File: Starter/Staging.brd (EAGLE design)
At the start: 20 x 20 mm, 2 parts, among them J1 DF40.30PIN.RECEPTACLE, J3 DF40.30PIN.HEADER

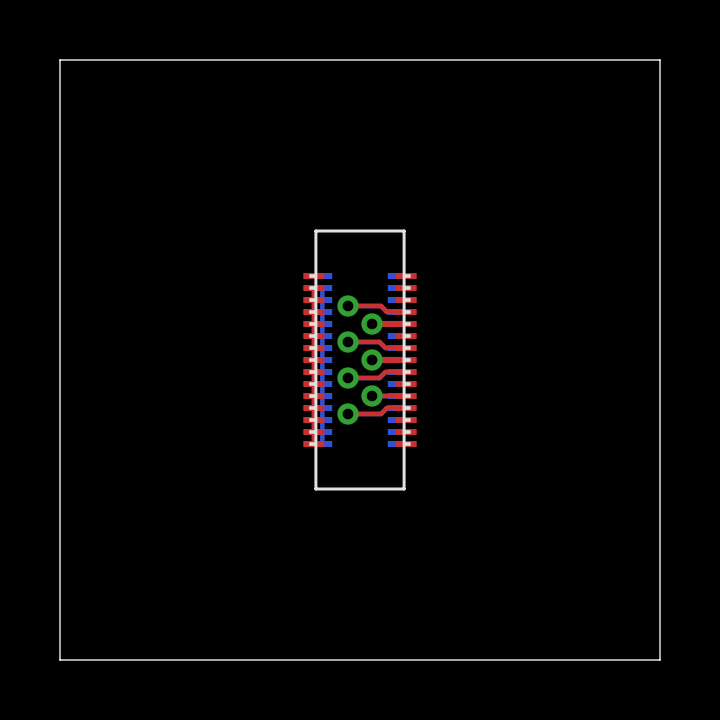
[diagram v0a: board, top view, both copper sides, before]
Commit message: More work on new headers. Focusing on H1, and it's various IO schemes.
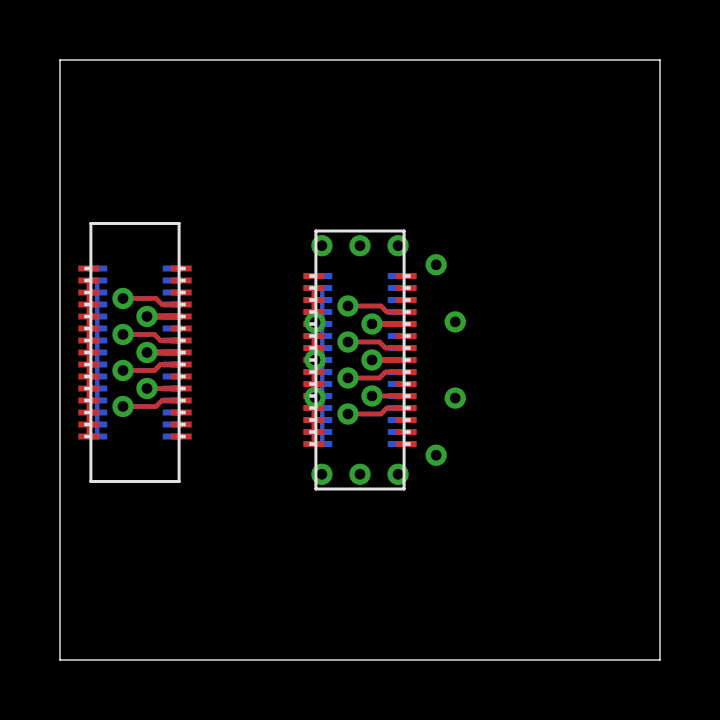
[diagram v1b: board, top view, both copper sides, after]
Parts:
- added H1: ROOT1.H1.BOTH.PASSTHROUGH, anomalousmaker:ROOT1.H1.BOTH
- moved J1 7.50 mm to (2.50, 10.2)
- moved J3 7.50 mm to (2.50, 10.2)
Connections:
- new net N$1: H1.IO.7.BOTTOM, H1.IO.7.TOP, H1.IO.7.VIA
- new net N$10: H1.GND@0.BOTTOM, H1.GND@0.TOP, H1.GND@0.VIA, H1.GND@1.BOTTOM, H1.GND@1.TOP, H1.GND@1.VIA, H1.GND@10.BOTTOM, H1.GND@10.TOP, H1.GND@11.BOTTOM, H1.GND@11.TOP, H1.GND@12.BOTTOM, H1.GND@12.TOP, H1.GND@13.BOTTOM, H1.GND@13.TOP, H1.GND@2.BOTTOM, H1.GND@2.TOP, H1.GND@2.VIA, H1.GND@3.BOTTOM, H1.GND@3.TOP, H1.GND@3.VIA, H1.GND@4.BOTTOM, H1.GND@4.TOP, H1.GND@5.BOTTOM, H1.GND@5.TOP, H1.GND@6.BOTTOM, H1.GND@6.TOP, H1.GND@7.BOTTOM, H1.GND@7.TOP, H1.GND@8.BOTTOM, H1.GND@8.TOP, H1.GND@9.BOTTOM, H1.GND@9.TOP
- new net N$11: H1.ADC0.BOTTOM, H1.ADC0.TOP, H1.ADC0.VIA
- new net N$12: H1.ADC1.BOTTOM, H1.ADC1.TOP, H1.ADC1.VIA
- new net N$13: H1.TX0.VIA, H1.TXO.BOTTOM, H1.TXO.TOP
- new net N$14: H1.RXI.BOTTOM, H1.RXI.TOP, H1.RXI.VIA
- new net N$15: H1.MOSI.BOTTOM, H1.MOSI.TOP, H1.MOSI.VIA
- new net N$16: H1.MISO.BOTTOM, H1.MISO.TOP, H1.MISO.VIA
- new net N$17: H1.SCLK.BOTTOM, H1.SCLK.TOP, H1.SCLK.VIA
- new net N$2: H1.IO.6.BOTTOM, H1.IO.6.TOP, H1.IO.6.VIA
- new net N$3: H1.IO.5.BOTTOM, H1.IO.5.TOP, H1.IO.5.VIA
- new net N$4: H1.IO.4.BOTTOM, H1.IO.4.TOP, H1.IO.4.VIA
- new net N$5: H1.IO.3.BOTTOM, H1.IO.3.TOP, H1.IO.3.VIA
- new net N$6: H1.IO.2.BOTTOM, H1.IO.2.TOP, H1.IO.2.VIA
- new net N$7: H1.IO.1.BOTTOM, H1.IO.1.TOP, H1.IO.1.VIA
- new net N$8: H1.IO.0.BOTTOM, H1.IO.0.TOP, H1.IO.0.VIA
- new net N$9: H1.!RST!.BOTTOM, H1.!RST!.TOP, H1.!RST!.VIA

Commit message: Created Test Module to test out Samtec SSH, STH, and SEI headers, along with EEPROM/Loki Scheme, and breakable PCB idea.
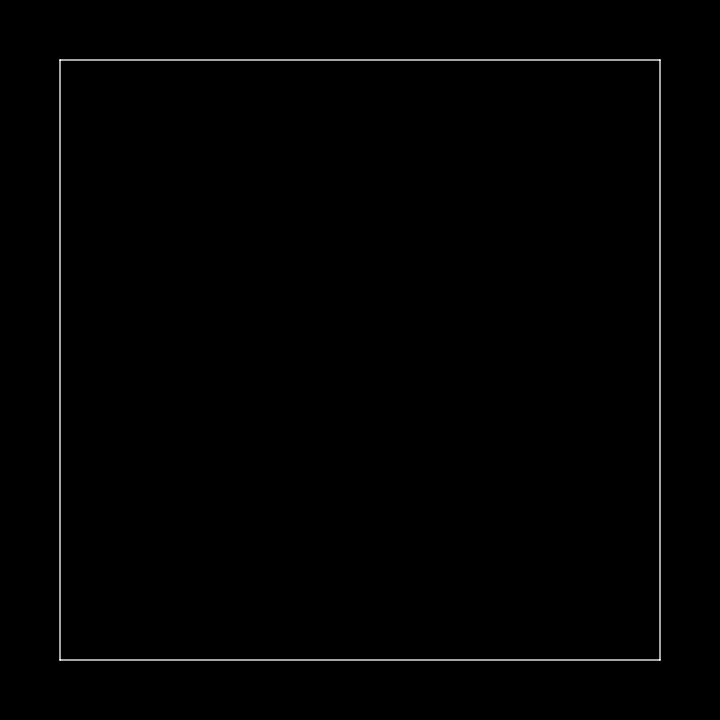
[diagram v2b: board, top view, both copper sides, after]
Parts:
- removed H1: ROOT1.H1.BOTH.PASSTHROUGH, anomalousmaker:ROOT1.H1.BOTH
- removed J1: DF40.30PIN.RECEPTACLE, hirose:DF40(XX)-30DS-0.4V
- removed J3: DF40.30PIN.HEADER, hirose:DF40(XX)-30DP-0.4V
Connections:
- removed net ADC0: J1.2, J3.30
- removed net ADC1: J1.4, J3.28
- removed net GND: J1.11, J1.13, J1.15, J1.17, J1.19, J1.21, J1.23, J1.25, J1.27, J1.29, J1.3, J1.5, J1.7, J1.9, J3.1, J3.11, J3.13, J3.15, J3.17, J3.19, J3.21, J3.23, J3.25, J3.27, J3.3, J3.5, J3.7, J3.9
- removed net IO.0: J1.16, J3.16
- removed net IO.1: J1.18, J3.14
- removed net IO.2: J1.20, J3.12
- removed net IO.3: J1.22, J3.10
- removed net IO.4: J1.24, J3.8
- removed net IO.5: J1.26, J3.6
- removed net IO.6: J1.28, J3.4
- removed net IO.7: J1.30, J3.2
- removed net MISO: J1.12, J3.20
- removed net MOSI: J1.10, J3.22
- removed net N$1: H1.IO.7.BOTTOM, H1.IO.7.TOP, H1.IO.7.VIA
- removed net N$10: H1.GND@0.BOTTOM, H1.GND@0.TOP, H1.GND@0.VIA, H1.GND@1.BOTTOM, H1.GND@1.TOP, H1.GND@1.VIA, H1.GND@10.BOTTOM, H1.GND@10.TOP, H1.GND@11.BOTTOM, H1.GND@11.TOP, H1.GND@12.BOTTOM, H1.GND@12.TOP, H1.GND@13.BOTTOM, H1.GND@13.TOP, H1.GND@2.BOTTOM, H1.GND@2.TOP, H1.GND@2.VIA, H1.GND@3.BOTTOM, H1.GND@3.TOP, H1.GND@3.VIA, H1.GND@4.BOTTOM, H1.GND@4.TOP, H1.GND@5.BOTTOM, H1.GND@5.TOP, H1.GND@6.BOTTOM, H1.GND@6.TOP, H1.GND@7.BOTTOM, H1.GND@7.TOP, H1.GND@8.BOTTOM, H1.GND@8.TOP, H1.GND@9.BOTTOM, H1.GND@9.TOP
- removed net N$11: H1.ADC0.BOTTOM, H1.ADC0.TOP, H1.ADC0.VIA
- removed net N$12: H1.ADC1.BOTTOM, H1.ADC1.TOP, H1.ADC1.VIA
- removed net N$13: H1.TX0.VIA, H1.TXO.BOTTOM, H1.TXO.TOP
- removed net N$14: H1.RXI.BOTTOM, H1.RXI.TOP, H1.RXI.VIA
- removed net N$15: H1.MOSI.BOTTOM, H1.MOSI.TOP, H1.MOSI.VIA
- removed net N$16: H1.MISO.BOTTOM, H1.MISO.TOP, H1.MISO.VIA
- removed net N$17: H1.SCLK.BOTTOM, H1.SCLK.TOP, H1.SCLK.VIA
- removed net N$2: H1.IO.6.BOTTOM, H1.IO.6.TOP, H1.IO.6.VIA
- removed net N$3: H1.IO.5.BOTTOM, H1.IO.5.TOP, H1.IO.5.VIA
- removed net N$4: H1.IO.4.BOTTOM, H1.IO.4.TOP, H1.IO.4.VIA
- removed net N$5: H1.IO.3.BOTTOM, H1.IO.3.TOP, H1.IO.3.VIA
- removed net N$6: H1.IO.2.BOTTOM, H1.IO.2.TOP, H1.IO.2.VIA
- removed net N$7: H1.IO.1.BOTTOM, H1.IO.1.TOP, H1.IO.1.VIA
- removed net N$8: H1.IO.0.BOTTOM, H1.IO.0.TOP, H1.IO.0.VIA
- removed net N$9: H1.!RST!.BOTTOM, H1.!RST!.TOP, H1.!RST!.VIA
- removed net RST: J1.1, J3.29
- removed net RXI: J1.8, J3.24
- removed net SCLK: J1.14, J3.18
- removed net TXO: J1.6, J3.26
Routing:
- net GND: track 10.4 -> 0.00 mm
- net RXI: track 3.76 -> 0.00 mm, vias 1 -> 0
- net IO.4: track 3.76 -> 0.00 mm, vias 1 -> 0
- net SCLK: track 3.76 -> 0.00 mm, vias 1 -> 0
- net IO.1: track 3.76 -> 0.00 mm, vias 1 -> 0
- net MOSI: track 2.00 -> 0.00 mm, vias 1 -> 0
- net IO.3: track 2.00 -> 0.00 mm, vias 1 -> 0
- net IO.0: track 2.00 -> 0.00 mm, vias 1 -> 0
